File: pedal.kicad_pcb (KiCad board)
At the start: 2 copper layers, 1 part, among them U1 STM32H745XIH6

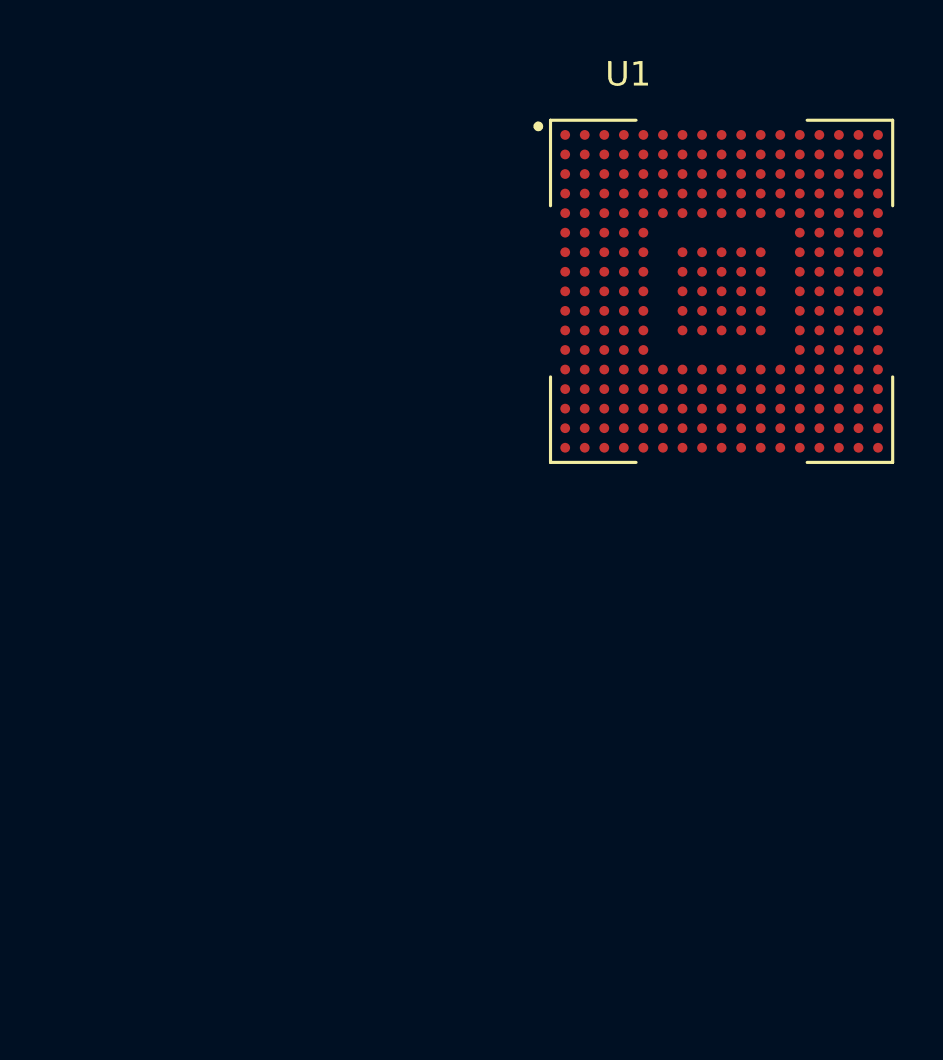
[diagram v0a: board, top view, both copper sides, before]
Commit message: Added TPS631000
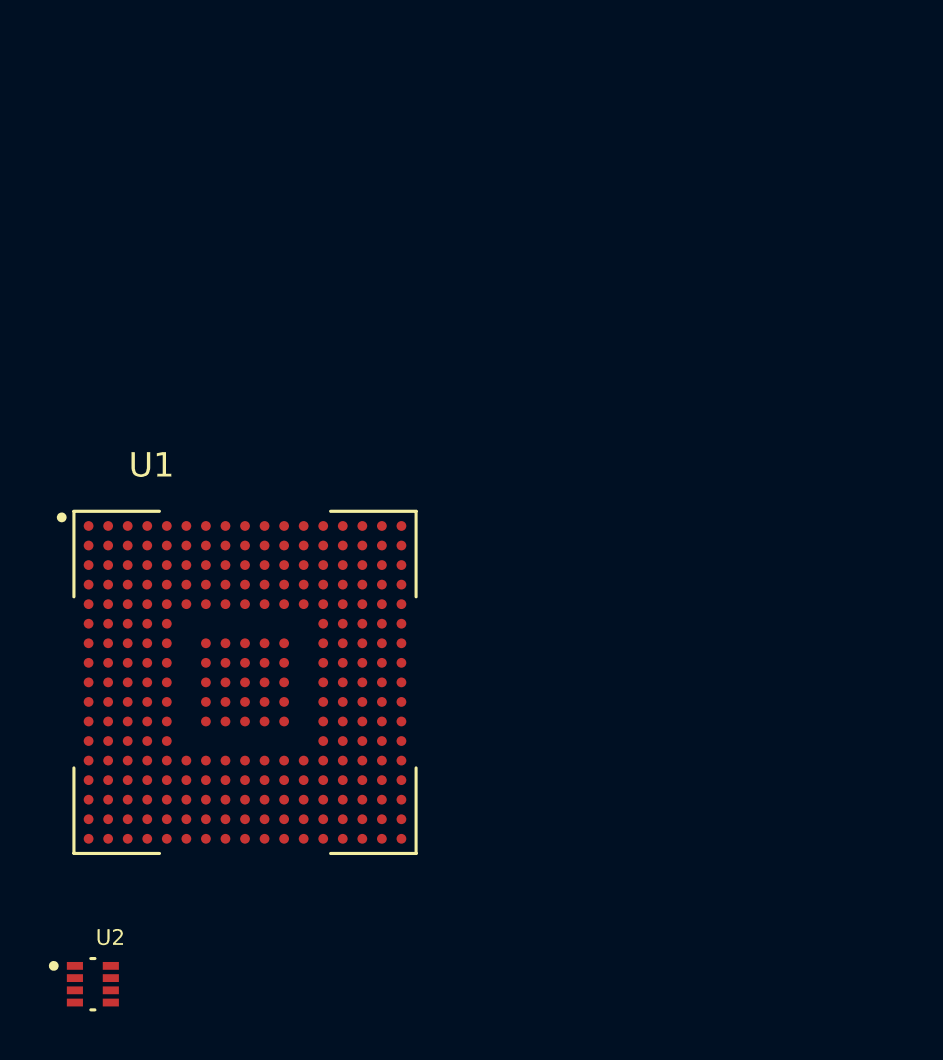
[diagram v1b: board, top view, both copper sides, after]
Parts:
- added U2: TPS631000DRLR, footprints:SOT50P160X60-8N, F.Cu at (112.8, 124.9)
- moved U1 25.2 mm to (119.0, 112.5)

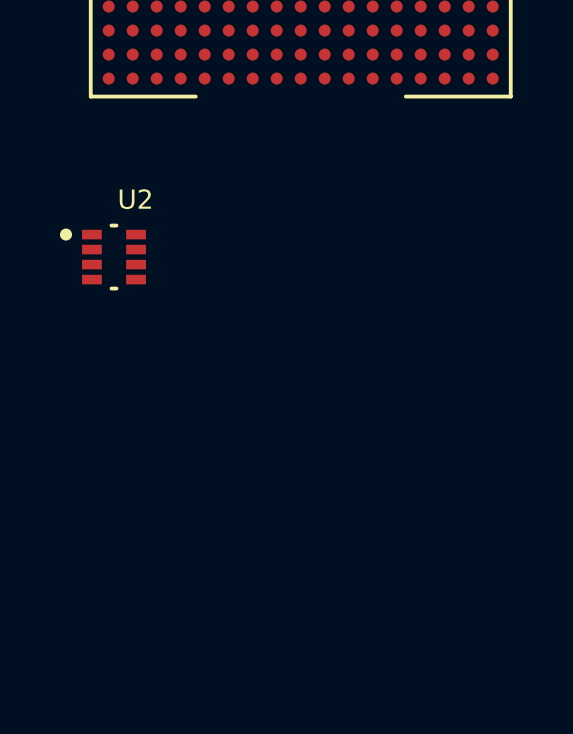
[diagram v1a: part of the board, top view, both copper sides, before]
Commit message: buck boost regulator schematic done
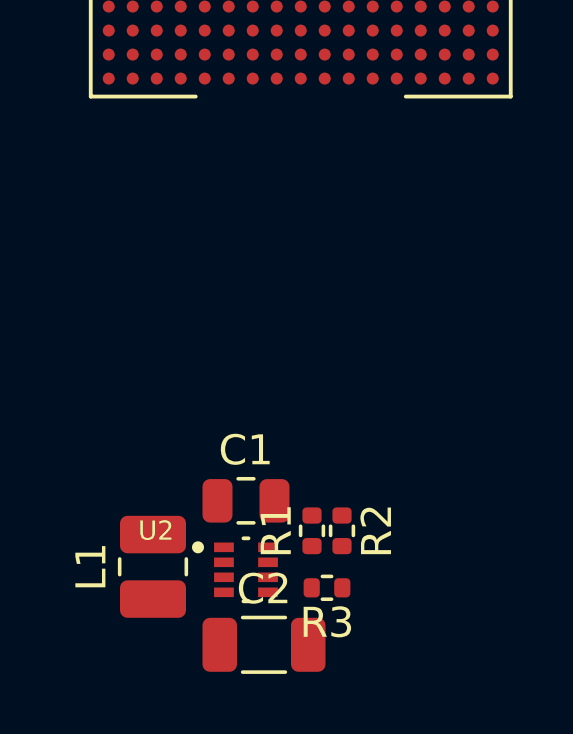
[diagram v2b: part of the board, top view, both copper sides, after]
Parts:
- added C1: 47uF, Capacitor_SMD:C_0805_2012Metric, F.Cu at (117.2, 133.0)
- added C2: 22uF, Capacitor_SMD:C_1206_3216Metric, F.Cu at (117.8, 137.8)
- added L1: 1uH, Inductor_SMD:L_1008_2520Metric, F.Cu at (114.1, 135.2)
- added R1: 91k, Resistor_SMD:R_0402_1005Metric, F.Cu at (119.4, 134.0)
- added R2: 511k, Resistor_SMD:R_0402_1005Metric, F.Cu at (120.4, 134.0)
- added R3: 91k, Resistor_SMD:R_0402_1005Metric, F.Cu at (119.9, 135.9)
- moved U2 11.3 mm to (117.2, 135.3)
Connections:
- U2 pad 1: unconnected-(U2-VOUT-Pad1) -> +3V3
- U2 pad 2: unconnected-(U2-LX2-Pad2) -> Net-(U2-LX2)
- U2 pad 3: unconnected-(U2-LX1-Pad3) -> Net-(U2-LX1)
- U2 pad 4: unconnected-(U2-VIN-Pad4) -> /Power path/VSYS
- U2 pad 5: unconnected-(U2-EN-Pad5) -> /Power path/VSYS
- U2 pad 6: unconnected-(U2-MODE-Pad6) -> /Power path/PS_MODE
- U2 pad 7: unconnected-(U2-GND-Pad7) -> GND
- U2 pad 8: unconnected-(U2-FB-Pad8) -> Net-(U2-FB)

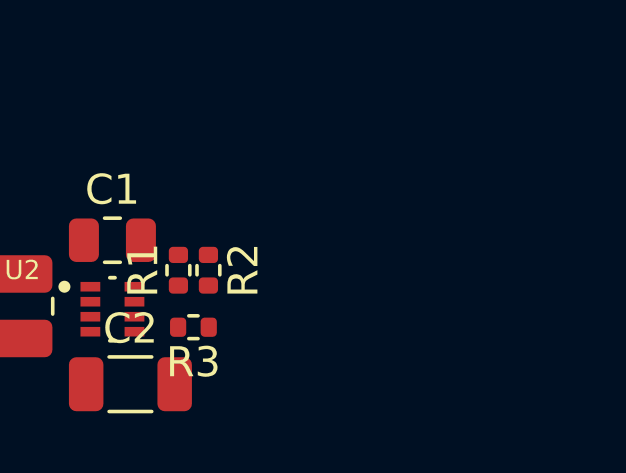
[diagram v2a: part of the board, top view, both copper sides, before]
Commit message: added LDO for LCD rail
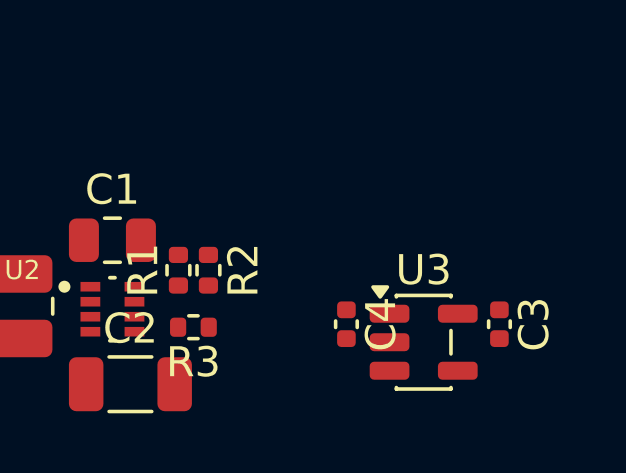
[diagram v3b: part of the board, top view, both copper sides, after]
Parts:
- added C3: 1uF, Capacitor_SMD:C_0402_1005Metric, F.Cu at (130.1, 135.8)
- added C4: 1uF, Capacitor_SMD:C_0402_1005Metric, F.Cu at (125.0, 135.8)
- added U3: TLV77018PDBVR, Package_TO_SOT_SMD:SOT-23-5, F.Cu at (127.6, 136.4)
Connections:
- C2 pad 1: /Power path/VSYS -> /Power path/VMUX
- U2 pad 4: /Power path/VSYS -> /Power path/VMUX

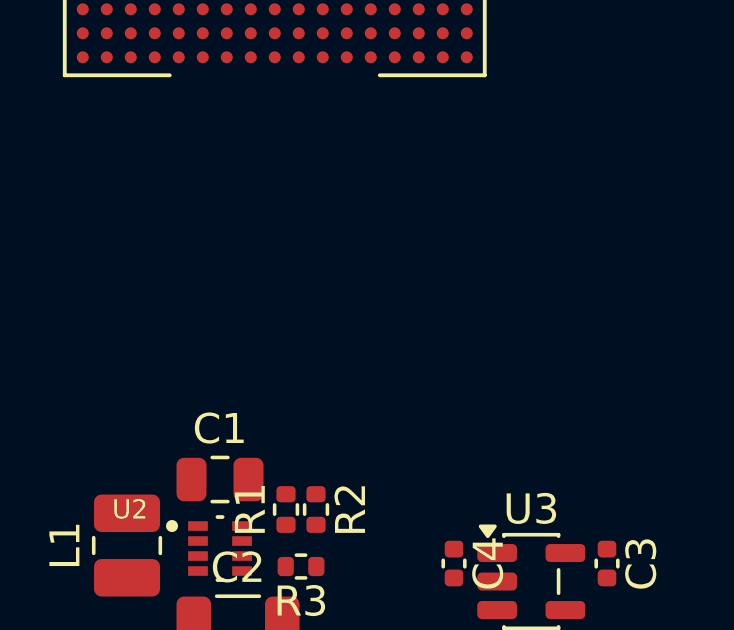
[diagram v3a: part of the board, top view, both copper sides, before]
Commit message: add tps2121 power mux component
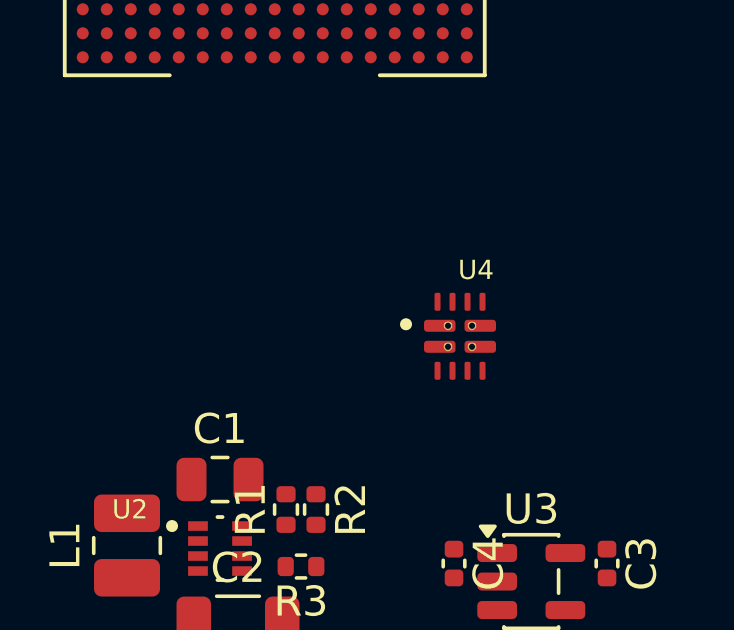
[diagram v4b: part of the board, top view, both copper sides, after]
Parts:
- added U4: TPS2121RUXR, footprints:IC_TPS2121RUXR, F.Cu at (125.2, 128.2)

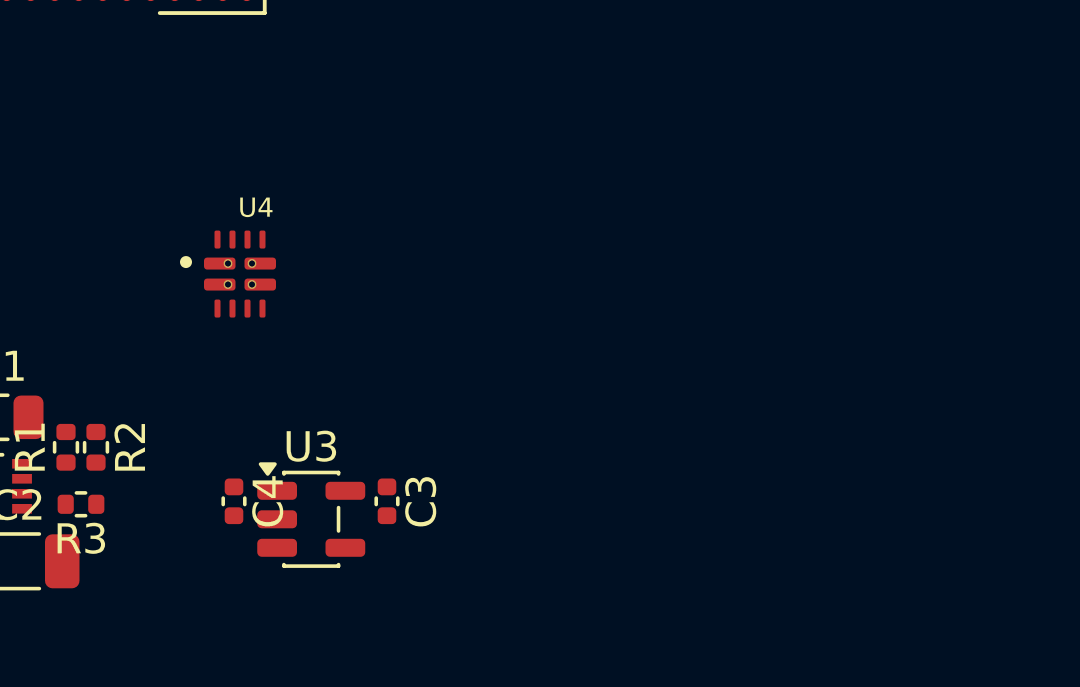
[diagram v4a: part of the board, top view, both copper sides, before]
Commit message: add type c receptacle
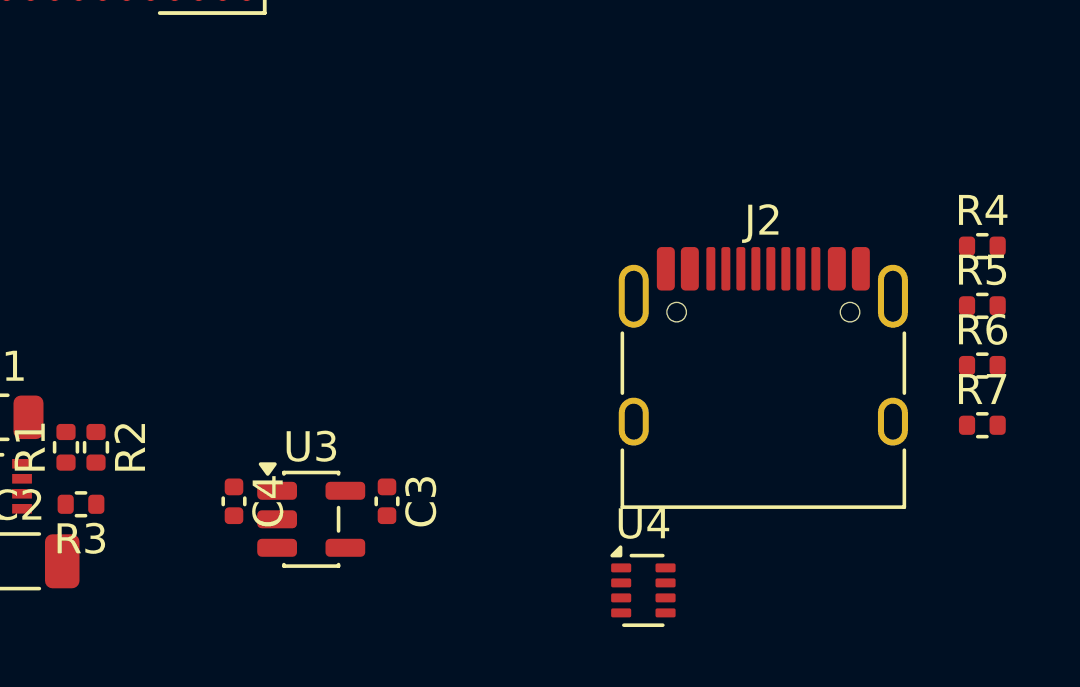
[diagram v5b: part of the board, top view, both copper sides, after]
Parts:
- added J2: USB_C_Receptacle_USB2.0_16P, Connector_USB:USB_C_Receptacle_HRO_TYPE-C-31-M-12, F.Cu at (142.6, 132.1)
- added R4: 300k, Resistor_SMD:R_0402_1005Metric, F.Cu at (149.9, 127.3)
- added R5: 91k, Resistor_SMD:R_0402_1005Metric, F.Cu at (149.9, 129.3)
- added R6: 5.1k, Resistor_SMD:R_0402_1005Metric, F.Cu at (149.9, 131.3)
- added R7: 5.1k, Resistor_SMD:R_0402_1005Metric, F.Cu at (149.9, 133.3)
- U4: value TPS2121RUXR -> TPS2116DRL; footprint footprints:IC_TPS2121RUXR -> Package_TO_SOT_SMD:SOT-583-8
- moved U4 17.1 mm to (138.6, 138.8)
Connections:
- net /Power path/PS_MODE renamed /Power path/MODE
- U2 pad 5: /Power path/VSYS -> /Power path/VMUX
- U4 pad 1: Net-(U4-OUT-Pad1) -> GND
- U4 pad 2: Net-(U4-IN2-Pad2) -> /Power path/VMUX
- U4 pad 3: unconnected-(U4-CP2-Pad3) -> /Power path/VUSB
- U4 pad 4: unconnected-(U4-OV2-Pad4) -> Net-(U4-PR1)
- U4 pad 5: unconnected-(U4-OV1-Pad5) -> /Power path/VUSB
- U4 pad 6: unconnected-(U4-PR1-Pad6) -> /Power path/VBATT
- U4 pad 7: Net-(U4-IN1-Pad7) -> /Power path/VMUX
- U4 pad 8: Net-(U4-OUT-Pad1) -> /Power path/MUX_STATE

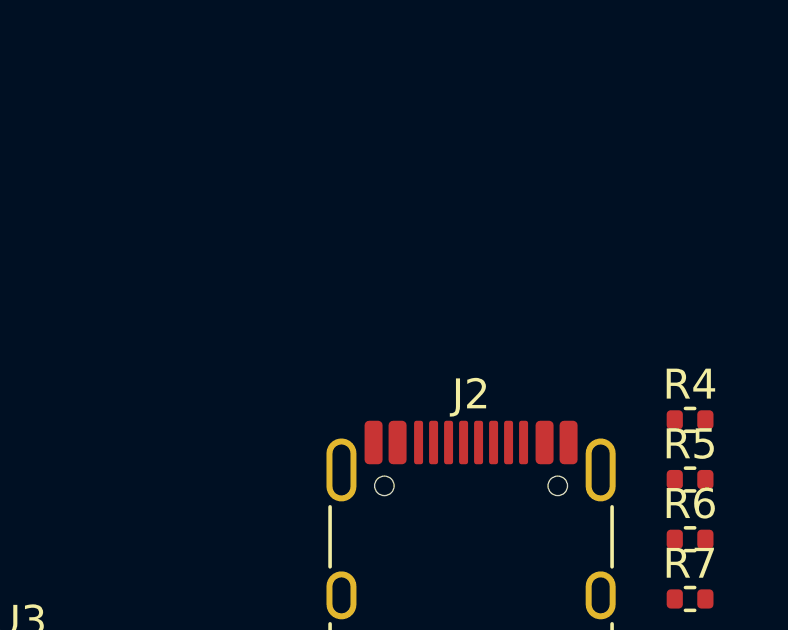
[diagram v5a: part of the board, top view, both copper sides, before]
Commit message: add esd protection to usb port
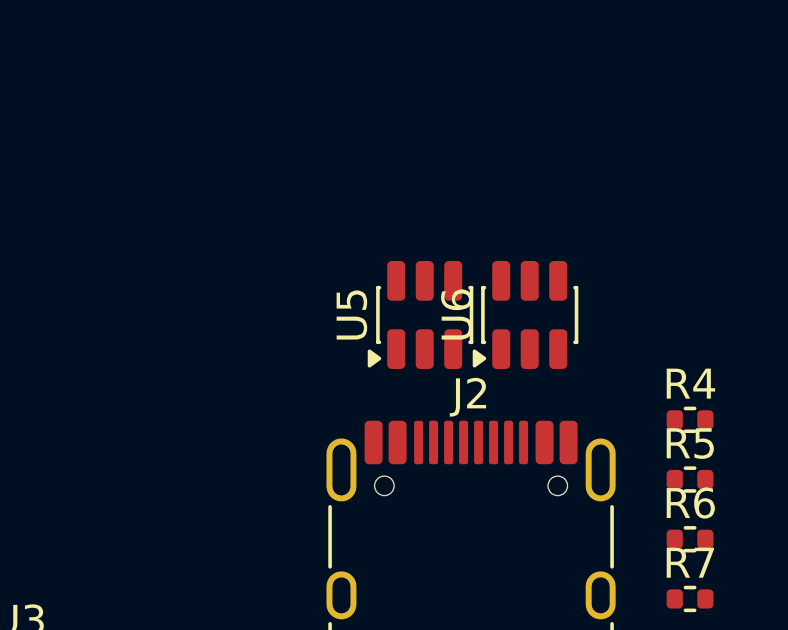
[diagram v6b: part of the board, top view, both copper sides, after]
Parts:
- added U5: USBLC6-2SC6, Package_TO_SOT_SMD:SOT-23-6, F.Cu at (141.1, 123.8)
- added U6: USBLC6-2SC6, Package_TO_SOT_SMD:SOT-23-6, F.Cu at (144.6, 123.8)

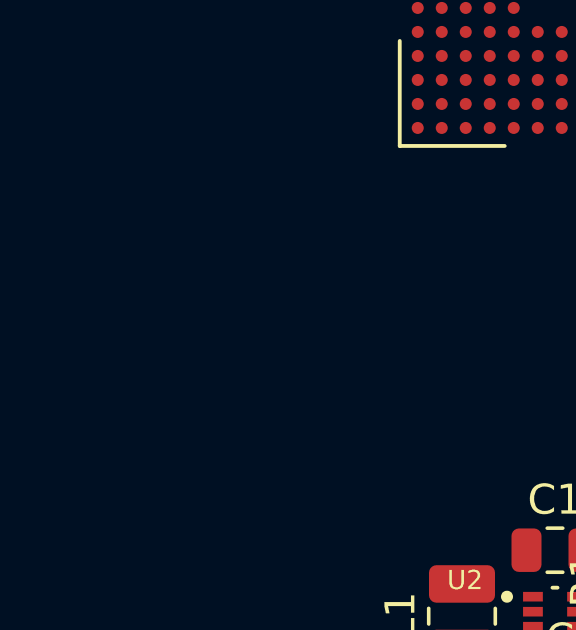
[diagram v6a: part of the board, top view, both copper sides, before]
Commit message: add bq25302 charger
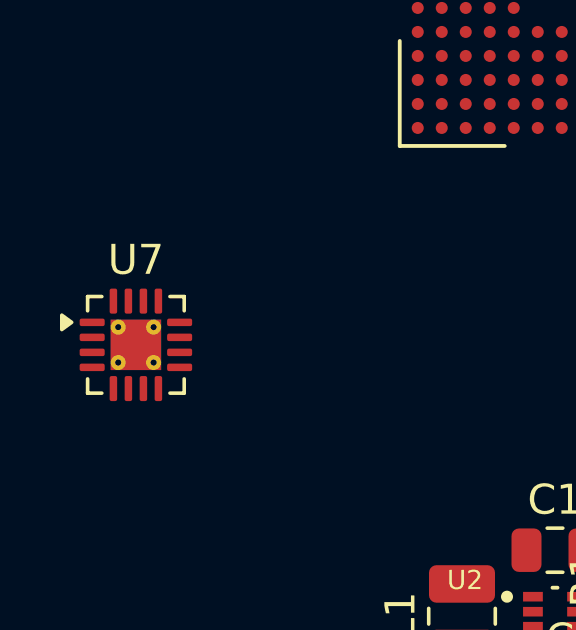
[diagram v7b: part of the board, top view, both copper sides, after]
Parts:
- added U7: ~, Package_DFN_QFN:WQFN-16-1EP_3x3mm_P0.5mm_EP1.68x1.68mm_ThermalVias, F.Cu at (103.2, 126.2)
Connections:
- U6 pad 2: unconnected-(U6-GND-Pad2) -> GND
- U6 pad 5: unconnected-(U6-VBUS-Pad5) -> /Power path/VUSB

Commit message: fuel gauge wip
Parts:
- added C5: 2.2uF, Capacitor_SMD:C_0603_1608Metric, F.Cu at (160.4, 119.7)
- added C6: 10uF, Capacitor_SMD:C_0603_1608Metric, F.Cu at (160.4, 122.2)
- added C7: 2.2uF, Capacitor_SMD:C_0603_1608Metric, F.Cu at (160.4, 124.7)
- added C8: 47nF, Capacitor_SMD:C_0603_1608Metric, F.Cu at (160.4, 127.2)
- added C9: 10uF, Capacitor_SMD:C_0603_1608Metric, F.Cu at (160.4, 129.7)
- added L2: 1uH, Inductor_SMD:L_1008_2520Metric, F.Cu at (164.9, 120.3)
- added R8: 27k, Resistor_SMD:R_0402_1005Metric, F.Cu at (163.9, 127.8)
- added R9: 200k, Resistor_SMD:R_0402_1005Metric, F.Cu at (163.9, 129.8)
- added U8: BQ27427YZFR, footprints:IC_BQ27427YZFR, F.Cu at (150.5, 114.6)
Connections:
- U7 pad 1: unconnected-(U7-VBUS-Pad1) -> /Power path/VUSB
- U7 pad 10: unconnected-(U7-BAT-Pad10) -> /Power path/VCELL
- U7 pad 11: Net-(U7-GND-Pad11) -> GND
- U7 pad 12: Net-(U7-GND-Pad11) -> GND
- U7 pad 15: unconnected-(U7-BTST-Pad15) -> Net-(U7-BTST)
- U7 pad 16: unconnected-(U7-PMID-Pad16) -> Net-(U7-PMID)
- U7 pad 17: unconnected-(U7-EPAD-Pad17) -> GND
- U7 pad 2: unconnected-(U7-REGN-Pad2) -> /Power path/REGN
- U7 pad 3: unconnected-(U7-STAT-Pad3) -> /Power path/CHARGER_STAT
- U7 pad 4: unconnected-(U7-ICHG-Pad4) -> Net-(U7-ICHG)
- U7 pad 6: unconnected-(U7-nEN-Pad6) -> /Power path/CHARGER_nEN
- U7 pad 7: unconnected-(U7-TS-Pad7) -> /Power path/BATT_TS
- U7 pad 8: unconnected-(U7-NC-Pad8) -> GND
- U7 pad 9: unconnected-(U7-VSET-Pad9) -> GND
